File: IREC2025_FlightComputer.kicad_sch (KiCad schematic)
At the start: 87 parts, among them J1 Molex Microfit, J2 BOOT0, J3 Companion, J4 Molex Microfit, J5 SWD, J6 Molex Microfit, Q1 SI7232DN-T1-GE3, U1 STM32U575VGTx, U10 XL4015E1, U5 LP5912Q3.3DRVRQ1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

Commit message: Feat: Replace old LDO with better LDO
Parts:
- added C39, C41: 10uF, PCM_JLCPCB:C_0603, symbol PCM_JLCPCB-Capacitors:1206,10uF
- added D10, D9: NRVB120VLSFT1G, EasyEDA:SOD-123_L2.7-W1.6-LS3.7-RD-1, symbol EasyEDA:NRVB120VLSFT1G
- added U13: TLV75733PDBV, Package_TO_SOT_SMD:SOT-23-5, symbol Regulator_Linear:TLV75733PDBV
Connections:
- net +3.3V: now also C39.1, U13.1 (IN), U13.3 (EN)
- net +5V: now also D10.2 (A)
- net GND: now also C39.2, C41.2, U13.2 (GND)
- net VBUS: now also D9.2 (A)
- new net: C41.1, D10.1 (K), D9.1 (K), U13.5 (OUT)
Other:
- moved on the sheet: C19, C2, C21, C29, C3, C31, C35, C37, C38, C74, D4, D5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

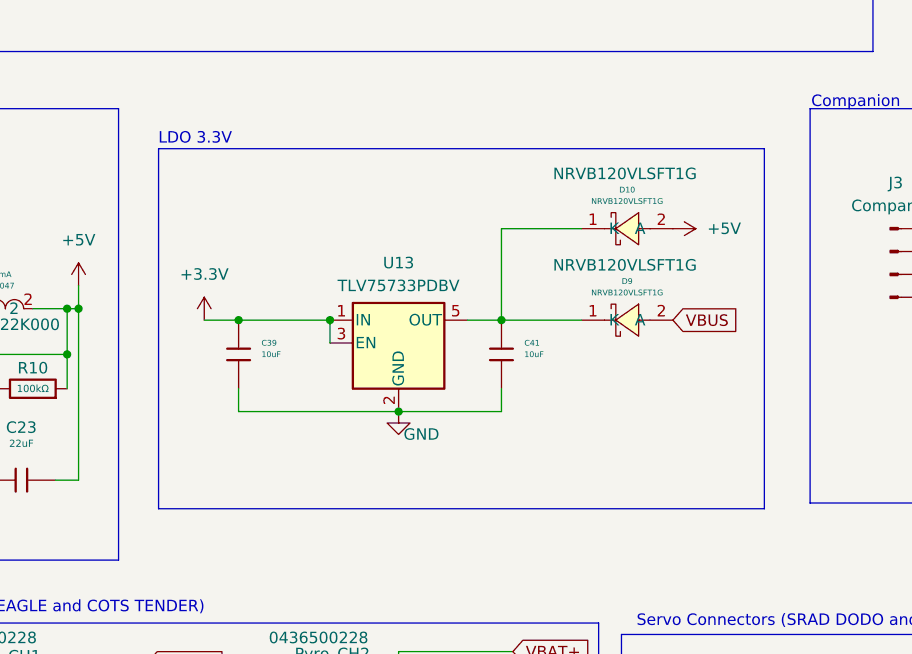
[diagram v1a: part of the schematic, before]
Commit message: Feat: Finish superior LDO route
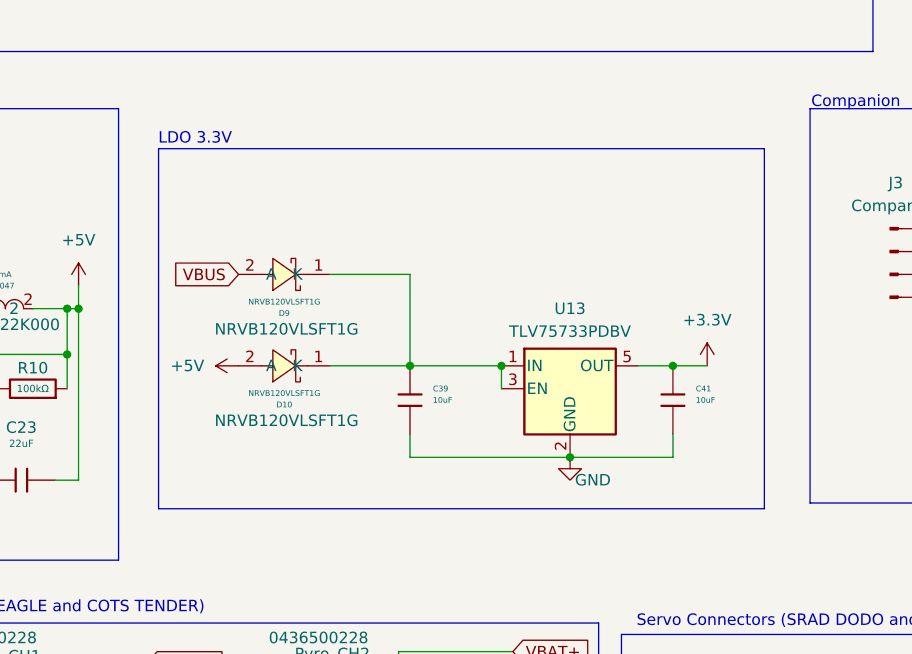
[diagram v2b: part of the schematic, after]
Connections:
- net +3.3V: now also C41.1, U13.5 (OUT); no longer C39.1, U13.1 (IN), U13.3 (EN)
- net at D10.1 (K), D9.1 (K): now also C39.1, U13.1 (IN), U13.3 (EN); no longer C41.1, U13.5 (OUT)
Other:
- moved on the sheet: C39, C41, D10, D9, U13

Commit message: Added silkscreen + Changed gps vbackup
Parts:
- removed C19, C37: 1uF, PCM_JLCPCB:C_0603, symbol PCM_JLCPCB-Capacitors:0402,1uF
- removed C2: 220UF 16V, EasyEDA:CAP-SMD_BD6.3-L6.6-W6.6-LS7.4-FD, symbol EasyEDA:220UF16V铝电解电容
- removed C21: 2.2uF, PCM_JLCPCB:C_0603, symbol PCM_JLCPCB-Capacitors:0402,2.2uF
- removed C29, C31: 100nF, PCM_JLCPCB:C_0603, symbol PCM_JLCPCB-Capacitors:0402,100nF
- removed C3: 470uF, Capacitor_SMD:CP_Elec_8x10, symbol PCM_JLCPCB-Capacitors:Plugin,D10xL16mm,470uF
- removed C35: 180uF, Capacitor_SMD:CP_Elec_5x5.3, symbol Device:C_Small
- removed C38: 100uF, Capacitor_SMD:CP_Elec_5x5.3, symbol PCM_JLCPCB-Capacitors:Plugin,D10xL16mm,470uF
- removed C74: 100uF, EasyEDA:CAP-SMD_L3.2-W1.6, symbol EasyEDA:T520A107M006ATE070
- removed D4, D5: NRVB120VLSFT1G, EasyEDA:SOD-123_L2.7-W1.6-LS3.7-RD-1, symbol EasyEDA:NRVB120VLSFT1G
- removed D7, D8: SS34_C466502, GNSS:DIOM7959X262N, symbol EasyEDA:SS34_C466502
- removed J4, J6: Molex Microfit, Connector_Molex:Molex_Micro-Fit_3.0_43650-0215_1x02_P3.00mm_Vertical, symbol Connector:Conn_01x02_Socket
- removed L2: 33uH,5A, Inductor_SMD:L_Bourns_SRR1208_12.7x12.7mm, symbol 33uHcoil:2107-H-RC
- removed L3: 33uH, Inductor_SMD:L_Bourns_SRP1038C_10.0x10.0mm, symbol Device:L
- removed R24: 3.3kΩ, PCM_JLCPCB:R_0603, symbol PCM_JLCPCB-Resistors:0603,3.3kΩ
- removed R8: 10kΩ, PCM_JLCPCB:R_0603, symbol PCM_JLCPCB-Resistors:0603,10kΩ
- removed U10: XL4015E1, EasyEDA:TO-263-5_L10.2-W8.9-P1.70-TL, symbol EasyEDA:XL4015E1
- removed U5: LP5912Q3.3DRVRQ1, EasyEDA:WSON-6_L2.0-W2.0-P0.65-TL-EP, symbol EasyEDA:LP5912Q3.3DRVRQ1
- removed U7: XL1509-5.0, Package_SO:SOIC-8_3.9x4.9mm_P1.27mm, symbol Regulator_Switching:XL1509-5.0
- L1: value 2.2uH,50mA -> 2.2uH,1A
- R16, R17: value 3.3kΩ -> 10kΩ; Digikey Parts RMCF0603JT3K30 -> RC0603FR-0710KL
- U13: Digikey Parts (none) -> TLV75733PDBVR
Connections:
- net BUZZER: now also U1.96 (PB9); no longer U1.40 (PE9)
- no-connect marks 16 -> 14

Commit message: adjustments
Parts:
- added C29, C31: 22uF, PCM_JLCPCB:C_0603, symbol PCM_JLCPCB-Capacitors:0603,22uF
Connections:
- net +5V: now also C29.2
- net GND: now also C29.1, C31.2
- net VBUS: now also C31.1

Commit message: Ordered version
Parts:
- added C2: 10uF, PCM_JLCPCB:C_0603, symbol PCM_JLCPCB-Capacitors:0402,100pF
- added C3: 100nF, PCM_JLCPCB:C_0603, symbol PCM_JLCPCB-Capacitors:0402,100pF
- added C37: 22uF, PCM_JLCPCB:C_0603, symbol PCM_JLCPCB-Capacitors:0603,22uF
- added J4: Molex Microfit, Connector_Molex:Molex_Micro-Fit_3.0_43650-0215_1x02_P3.00mm_Vertical, symbol Connector:Conn_01x02_Socket
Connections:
- net GND: now also C2.1, C3.1, C37.2, J4.1 (Pin_1)
- net at L1.1, U8.1 (SW), U8.2 (SW)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: now also C37.1
- net +5Vservo renamed ServoPow
- net ServoPow: now also C2.2, C3.2, J4.2 (Pin_2)

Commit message: fixes
Fixed mmc, power
Added external 5V Supply
Added external reset button
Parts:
- removed C29, C37: 22uF, PCM_JLCPCB:C_0603, symbol PCM_JLCPCB-Capacitors:0603,22uF
- removed R38: 10kΩ, PCM_JLCPCB:R_0603, symbol PCM_JLCPCB-Resistors:0402,10kΩ
- added D11: NRVB120VLSFT1G, EasyEDA:SOD-123_L2.7-W1.6-LS3.7-RD-1, symbol EasyEDA:NRVB120VLSFT1G
- added J7: Molex Microfit, Connector_Molex:Molex_Micro-Fit_3.0_43650-0215_1x02_P3.00mm_Vertical, symbol Connector:Conn_01x02_Socket
- added SW1: SKRKAEE020, EasyEDA:SW-SMD_L3.9-W3.0-P4.45, symbol EasyEDA:SKRKAEE020
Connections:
- net +5V: now also D11.2 (A), J7.2 (Pin_2)
- net GND: now also J7.1 (Pin_1), SW1.2
- net nRST: now also SW1.1
- net VBUSout: now reaches C39.1, D10.1 (K), D9.1 (K), U13.1 (IN), U13.3 (EN)
- net VBUSout: now also D11.1 (K)
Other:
- moved on the sheet: R9

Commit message: lmao
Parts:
- removed D11: NRVB120VLSFT1G, EasyEDA:SOD-123_L2.7-W1.6-LS3.7-RD-1, symbol EasyEDA:NRVB120VLSFT1G
- added J6: Conn_01x03_Pin, Connector_PinHeader_2.54mm:PinHeader_1x03_P2.54mm_Vertical, symbol Connector:Conn_01x03_Pin
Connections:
- net VBUSout is gone; now on net +5V: C39.1, D10.1 (K), D9.1 (K), U13.1 (IN), U13.3 (EN)
- net GND: now also J6.3 (Pin_3)
- net GNSS_RX: now also J6.1 (Pin_1)
- net GNSS_TX: now also J6.2 (Pin_2)
- net VBAT+: no longer Pyro_CH1.1 (Pin_1), Pyro_CH2.2 (Pin_2)
- net PYRO: now reaches D3.2, J1.2 (Pin_2)
- net PYRO: now also Pyro_CH1.1 (Pin_1), Pyro_CH2.2 (Pin_2)
